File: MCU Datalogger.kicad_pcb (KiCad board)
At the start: 4 copper layers, 48.6 x 32 mm, 30 parts, among them J1 Conn_01x04_Pin, J2 Conn_01x09_Pin, J3 Conn_01x04_Pin, J4 Conn_02x03_Odd_Even, U1 24LC1025, U2 24LC1025, U3 DS1337S_, U4 ATMEGA328P-AU, Y1 32.768 KHz, Y2 16 MHz

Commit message: added board characteristics.
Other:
- board text added: "0.2000 mm / 0.0000 mm"
- board text added: "0.3000 mm"
- board text added: "1.6000 mm"
- board text added: "48.6540 mm x 31.9848 mm"
- board text added: "BOARD CHARACTERISTICS"
- board text added: "Board Thickness:"
- board text added: "Board overall dimensions:"
- board text added: "Castellated pads:"
- board text added: "Copper Finish:"
- board text added: "Copper Layer Count:"
- board text added: "Edge card connectors:"
- board text added: "Impedance Control:"
- board text added: "Min hole diameter:"
- board text added: "Min track/spacing:"
- board text added: "No"
- board text added: "None"
- board text added: "Plated Board Edge:"

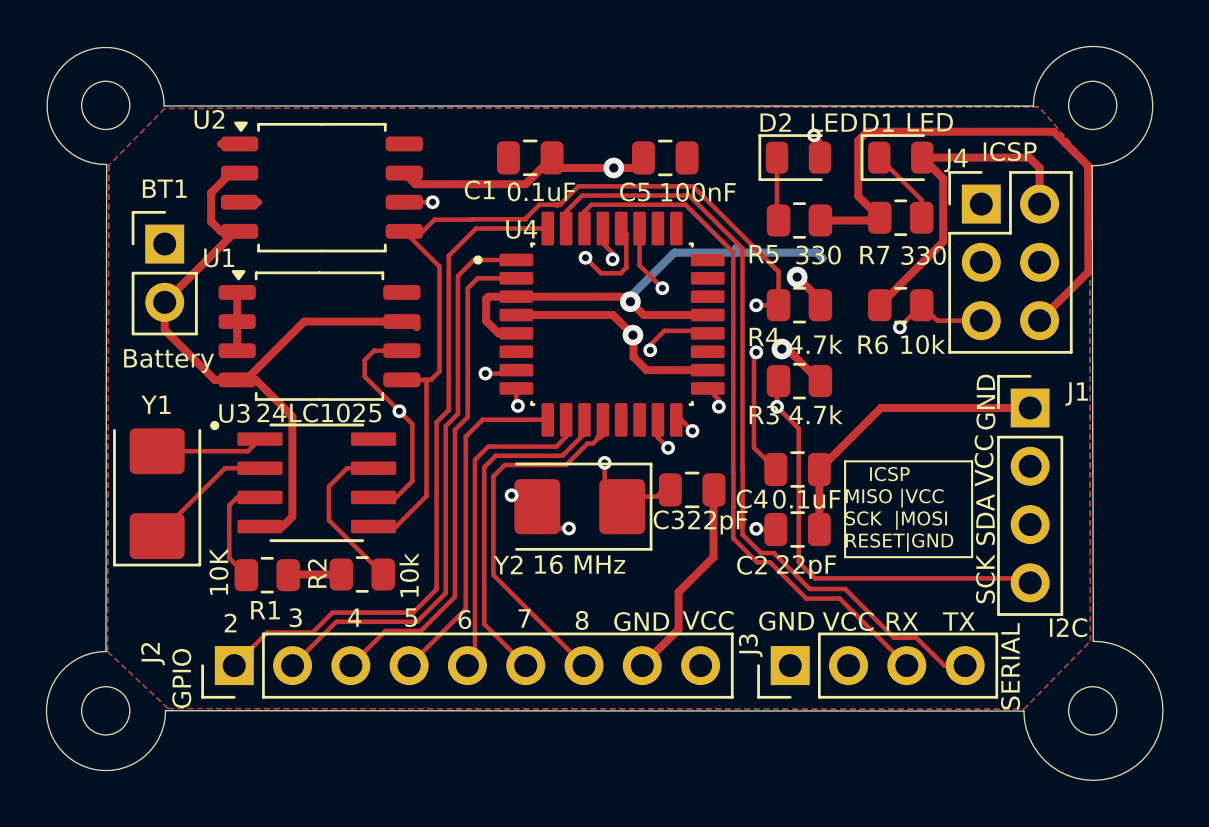
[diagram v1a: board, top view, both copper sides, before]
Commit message: gixing bugs in 4layer branch pcb .
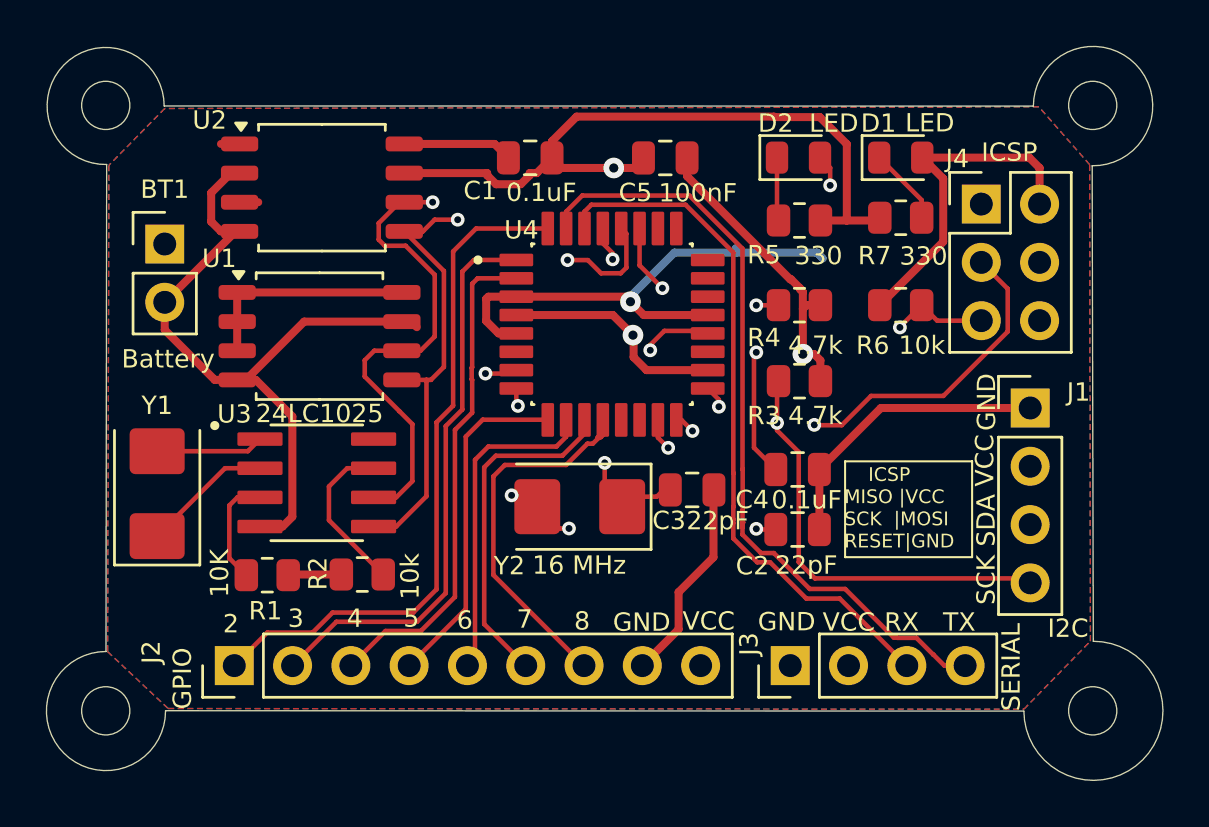
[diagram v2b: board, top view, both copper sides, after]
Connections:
- J1 pad 4: /SCK -> /SCL
- R3 pad 2: /SCK -> /SCL
- U1 pad 6: /SCK -> /SCL
- U2 pad 6: /SCK -> /SCL
- U3 pad 6: /SCK -> /SCL
- U4 pad 28: /SCK -> /SCL
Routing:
- net /SCK: track 96.2 -> 28.5 mm, vias 6 -> 3
- net /SCL: track 0.00 -> 65.3 mm, vias 0 -> 3
- net /Vcc: track 52.1 -> 75.5 mm, vias 3 -> 2
- net /SDA: track 69.2 -> 61.9 mm, vias 2 -> 3
- net GND: track 112.8 -> 108.9 mm
- net /MISO: track 19.2 -> 19.9 mm

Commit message: correction in back silkscreen .
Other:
- board text added: "v1.0 4 Layers desgin"
- board text removed: "v1.0 2 Layers desgin"
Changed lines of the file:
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@@
 		)
 	)
-	(gr_text "v1.0 \n2 Layers desgin"
+	(gr_text "v1.0 \n4 Layers desgin"
 		(at 149.09 106.055 0)
 		(layer "B.SilkS")
